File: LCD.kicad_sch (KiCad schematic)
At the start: 13 parts, among them IC3 LED_Driver_TPS61165DBVR, J5 IM2_Jumper, J6 IM1_Jumper, J8 IM0_Jumper

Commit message: Update
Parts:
- C30, C33, C40, C41, C52: footprint Capacitor_SMD:C_0805_2012Metric_Pad1.18x1.45mm_HandSolder -> Capacitor_SMD:C_0805_2012Metric
- R10: footprint Resistor_SMD:R_0805_2012Metric_Pad1.20x1.40mm_HandSolder -> Resistor_SMD:R_0805_2012Metric_1
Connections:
- net +3.3V is gone; now on net 3V3_BK4+: J5.1 (Pin_1), J6.1 (Pin_1), J8.1 (Pin_1)
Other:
- note added: "VCC"
- note added: "VCCIO"

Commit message: Update
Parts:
- removed C30: 1u, Capacitor_SMD:C_0805_2012Metric, symbol Device:C
- removed C33, C52: 4u7, Capacitor_SMD:C_0805_2012Metric, symbol Device:C
- removed C40: 220n, Capacitor_SMD:C_0805_2012Metric, symbol Device:C
- removed C41: 100n, Capacitor_SMD:C_0805_2012Metric, symbol Device:C
- removed D3: MBR0540T1G, Personal_Project:MBR0540T3G_SOD3716X135N, symbol Device:D
- removed FFC1: FFC_ZF5S-40-02-T-WT, Personal_Project:FFC_ZF5S-40-02-T-WT, symbol Personal_Projects:FFC_ZF5S-40-02-T-WT
- removed IC3: LED_Driver_TPS61165DBVR, Personal_Project:LEDDriver_TPS61165DBVR_SOT95P280X145-6N, symbol Personal_Projects:LED_Driver_TPS61165DBVR
- removed J5: IM2_Jumper, Connector_PinHeader_2.54mm:PinHeader_1x03_P2.54mm_Vertical, symbol Connector_Generic:Conn_01x03
- removed J6: IM1_Jumper, Connector_PinHeader_2.54mm:PinHeader_1x03_P2.54mm_Vertical, symbol Connector_Generic:Conn_01x03
- removed J8: IM0_Jumper, Connector_PinHeader_2.54mm:PinHeader_1x03_P2.54mm_Vertical, symbol Connector_Generic:Conn_01x03
- removed L1: Inductor_VLCF5020T-100M1R1-1, Personal_Project:Inductor_VLCF5020, symbol Personal_Projects:Inductor_VLCF5020T-100M1R1-1
- removed R10: 1R8, Resistor_SMD:R_0805_2012Metric_1, symbol Device:R
- added J9: BTB_10132798-062100LF, Personal_Project:BTB_AMPHENOL_10132798-062100LF, symbol Personal_Projects:BTB_10132798-062100LF
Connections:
- net 3V3_BK4+: now also J9.59, J9.60
- net FMC_A0: now also J9.30
- net FMC_D0: now also J9.10
- net FMC_D1: now also J9.11
- net FMC_D10: now also J9.24
- net FMC_D11: now also J9.25
- net FMC_D12: now also J9.1
- net FMC_D13: now also J9.2
- net FMC_D14: now also J9.3
- net FMC_D15: now also J9.5
- net FMC_D2: now also J9.13
- net FMC_D3: now also J9.14
- net FMC_D4: now also J9.16
- net FMC_D5: now also J9.17
- net FMC_D6: now also J9.18
- net FMC_D7: now also J9.20
- net FMC_D8: now also J9.21
- net FMC_D9: now also J9.22
- net FMC_NE1: now also J9.29
- net FMC_NOE: now also J9.6
- net FMC_NWE: now also J9.26
- net GND: now also J9.12, J9.15, J9.19, J9.23, J9.27, J9.31, J9.32, J9.33, J9.34, J9.35, J9.36, J9.37, J9.38, J9.39, J9.4, J9.40, J9.41, J9.42, J9.43, J9.44, J9.45, J9.46, J9.47, J9.48, J9.49, J9.50, J9.51, J9.52, J9.53, J9.54, J9.55, J9.56, J9.57, J9.58, J9.9, J9.SH1, J9.SH2
- net LCD_RESET: now also J9.7
- net LCD_TE: now also J9.28
- net LED_Driver_CTRL: now also J9.8
- no-connect marks 6 -> 0
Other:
- note removed: "CTRL PIN (Dimming mode - digital) The default dimming mode is PWM dimming. To enter 1 wire mode, the following digital pattern on the CTRL pin must be recognized by the device every time the device starts from the shutdown mode. 1. Pull CTRL pin high to enable the TPS61165, and to start the 1wire detection window. 2. After the EasyScale detection delay (tes_delay, 100 μs) expires, drive CTRL low 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"
- note removed: "Chip Selection Pin"
- note removed: "Compared to TN (Twisted Nematic) displays, IPS panels look much better when viewed from the side or at an angle - which is important for user interfaces on handheld or embedded devices. TE Pin When enabled via a command (usually 0x35), the TE pin outputs a pulse or level: Rising edge or level indicates it's safe to update GRAM (internal display RAM). You can wait for TE before sending new pixel d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"
- note removed: "Connect TE to a GPIO or external interrupt pin"
- note removed: "Connector for www.aliexpress.com/item/1005008632320232.html ILI9488 LCD, SSD1963"
- note removed: "Display Data/Command Selection Pin (L:Command, H: Data)"
- note removed: "IM0, IM1, IM2 to set the interface mode 8080 parallel or SPI"
- note removed: "MBR0540T1G"
- note removed: "NC Using capacitive touch"
- note removed: "R_SET = 200 mV / 120 mA = 1.67 Ω (use 1.6 Ω or 1.8 Ω standard)"
- note removed: "Read Enable In MCU Parallel Interface"
- note removed: "SOT-23"
- note removed: "To GPIO"
- note removed: "VCC"
- note removed: "VCCIO"
- note removed: "Was 5V on reference design"
- note removed: "Write Enable In MCU Parallel Interface"

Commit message: Update
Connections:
- net FMC_A0 is gone; now on net FMC_D7: J9.30
- net FMC_NE1 is gone; now on net FMC_D6: J9.29
- net FMC_D1: now also J9.12; no longer J9.11
- net FMC_D10: now also J9.56; no longer J9.24
- net FMC_D11: now also J9.52; no longer J9.25
- net FMC_D2: now also J9.14; no longer J9.13
- net FMC_D3: now also J9.16; no longer J9.14
- net FMC_D4: now also J9.22; no longer J9.16
- net FMC_D5: now also J9.24; no longer J9.17
- net FMC_D6: no longer J9.18
- net FMC_D7: no longer J9.20
- net FMC_D8: now also J9.59; no longer J9.21
- net FMC_D9: now also J9.58; no longer J9.22
- net FMC_NOE: now also J9.35; no longer J9.6
- net FMC_NWE: now also J9.27; no longer J9.26
- net GND: now also J9.11, J9.13, J9.17, J9.21, J9.25, J9.26, J9.28, J9.6; no longer J9.12, J9.19, J9.27, J9.31, J9.33, J9.35, J9.52, J9.56, J9.58
- net LCD_TE: now also J9.33; no longer J9.28
- net LED_Driver_CTRL: now also J9.31; no longer J9.8
- net 3V3_BK4+ renamed FMC_NE3
- net FMC_NE3: no longer J9.59
- new net FMC_A9: J9.8
- new net SMPS_OUT2_3V3+: J9.18, J9.19, J9.20

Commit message: Update
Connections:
- net GND: now also J9.7; no longer J9.46
- net LCD_RESET: now also J9.46; no longer J9.7
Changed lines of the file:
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@@
+	)
+	(junction
+		(at 176.53 113.03)
+		(diameter 0)
+		(color 0 0 0 0)
 	)
 	(junction
@@
 	)
 	(junction
-		(at 259.08 135.89)
-		(diameter 0)
-		(color 0 0 0 0)
-	)
-	(junction
 		(at 259.08 171.45)
 		(diameter 0)
@@
 	(wire
 		(pts
-			(xy 214.63 135.89) (xy 259.08 135.89)
-		)
-		(stroke
-			(width 0)
-			(type default)
-		)
-	)
-	(wire
-		(pts
 			(xy 199.39 179.07) (xy 199.39 181.61)
 		)
@@
 	(wire
 		(pts
-			(xy 259.08 135.89) (xy 259.08 138.43)
+			(xy 259.08 133.35) (xy 259.08 138.43)
 		)
 		(stroke
@@
 	(wire
 		(pts
-			(xy 259.08 133.35) (xy 259.08 135.89)
+			(xy 214.63 135.89) (xy 229.87 135.89)
 		)
 		(stroke
@@
 	(wire
 		(pts
+			(xy 176.53 113.03) (xy 176.53 115.57)
+		)
+		(stroke
+			(width 0)
+			(type default)
+		)
+	)
+	(wire
+		(pts
 			(xy 259.08 181.61) (xy 259.08 182.88)
 		)
@@
 	(wire
 		(pts
-			(xy 189.23 115.57) (xy 172.72 115.57)
+			(xy 189.23 115.57) (xy 176.53 115.57)
 		)
 		(stroke
@@
 	(wire
 		(pts
+			(xy 176.53 113.03) (xy 172.72 113.03)
+		)
+		(stroke
+			(width 0)
+			(type default)
+		)
+	)
+	(wire
+		(pts
 			(xy 259.08 140.97) (xy 259.08 143.51)
 		)
@@
 	(wire
 		(pts
-			(xy 189.23 113.03) (xy 172.72 113.03)
+			(xy 189.23 113.03) (xy 176.53 113.03)
 		)
 		(stroke
@@
 		)
 	)
+	(label "LCD_RESET"
+		(at 229.87 135.89 180)
+		(fields_autoplaced yes)
+		(effects
+			(font
+				(size 1.27 1.27)
+			)
+			(justify right bottom)
+		)
+	)
 	(label "FMC_D7"
 		(at 172.72 173.99 0)
@@
 	(label "FMC_D12"
 		(at 172.72 100.33 0)
-		(fields_autoplaced yes)
-		(effects
-			(font
-				(size 1.27 1.27)
-			)
-			(justify left bottom)
-		)
-	)
-	(label "LCD_RESET"
-		(at 172.72 115.57 0)
 		(fields_autoplaced yes)
 		(effects
@@
 	(hierarchical_label "LCD_RESET"
 		(shape bidirectional)
-		(at 172.72 115.57 180)
-		(fields_autoplaced yes)
-		(effects
-			(font
-				(size 1.27 1.27)
-			)
-			(justify right)
-		)
-	)
+		(at 229.87 135.89 0)
+		(fields_autoplaced yes)
+		(effects
+			(font
+				(size 1.27 1.27)
+			)
+			(justify left)
+		)
+	)

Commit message: Update
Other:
- company: (none) -> Peter Hancak
- title: (none) -> STM32H7S3 Board
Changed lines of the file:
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@@
 	(generator_version "8.0")
 	(paper "A3")
+	(title_block
+		(title "STM32H7S3 Board")
+		(date "2026-03-17")
+		(rev "B")
+		(company "Peter Hancak")
+	)
 	(junction
 		(at 259.08 151.13)

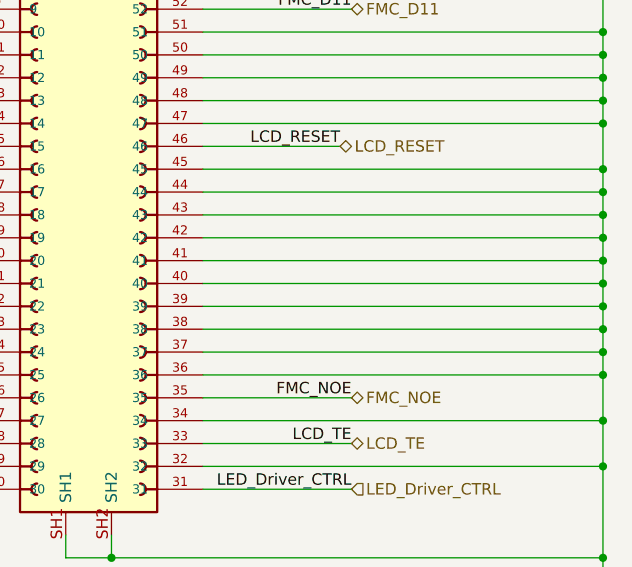
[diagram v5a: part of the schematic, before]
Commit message: Added I2C to the LCD interface
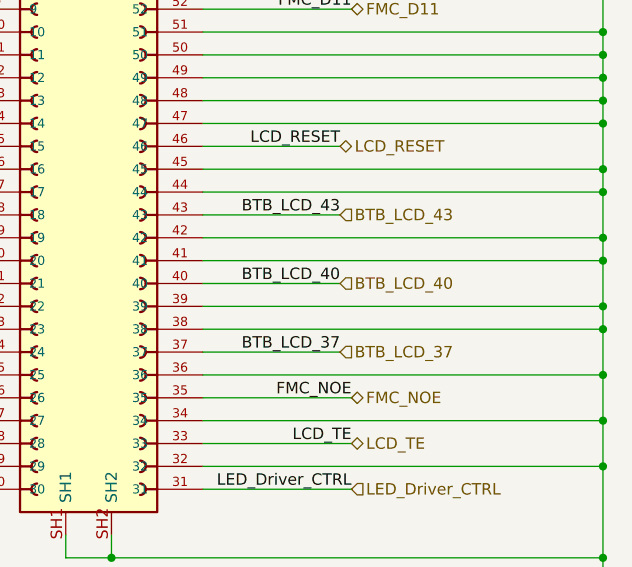
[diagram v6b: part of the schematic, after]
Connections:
- net GND: no longer J9.37, J9.40, J9.43
- new net BTB_LCD_37: J9.37
- new net BTB_LCD_40: J9.40
- new net BTB_LCD_43: J9.43
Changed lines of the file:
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@@
-	)
-	(junction
-		(at 259.08 151.13)
-		(diameter 0)
-		(color 0 0 0 0)
 	)
 	(junction
@@
 	)
 	(junction
-		(at 259.08 143.51)
-		(diameter 0)
-		(color 0 0 0 0)
-	)
-	(junction
 		(at 259.08 118.11)
 		(diameter 0)
@@
 	)
 	(junction
-		(at 259.08 158.75)
-		(diameter 0)
-		(color 0 0 0 0)
-	)
-	(junction
 		(at 259.08 153.67)
 		(diameter 0)
@@
 	(wire
 		(pts
-			(xy 259.08 158.75) (xy 259.08 161.29)
+			(xy 259.08 156.21) (xy 259.08 161.29)
 		)
 		(stroke
@@
 	(wire
 		(pts
+			(xy 214.63 143.51) (xy 229.87 143.51)
+		)
+		(stroke
+			(width 0)
+			(type default)
+		)
+	)
+	(wire
+		(pts
 			(xy 199.39 179.07) (xy 199.39 181.61)
 		)
@@
 	(wire
 		(pts
-			(xy 259.08 143.51) (xy 259.08 146.05)
-		)
-		(stroke
-			(width 0)
-			(type default)
-		)
-	)
-	(wire
-		(pts
 			(xy 189.23 107.95) (xy 172.72 107.95)
 		)
@@
 	(wire
 		(pts
-			(xy 259.08 151.13) (xy 259.08 153.67)
-		)
-		(stroke
-			(width 0)
-			(type default)
-		)
-	)
-	(wire
-		(pts
-			(xy 214.63 151.13) (xy 259.08 151.13)
+			(xy 259.08 148.59) (xy 259.08 153.67)
 		)
 		(stroke
@@
 	(wire
 		(pts
+			(xy 214.63 158.75) (xy 229.87 158.75)
+		)
+		(stroke
+			(width 0)
+			(type default)
+		)
+	)
+	(wire
+		(pts
 			(xy 189.23 110.49) (xy 172.72 110.49)
 		)
@@
 	(wire
 		(pts
+			(xy 214.63 140.97) (xy 259.08 140.97)
+		)
+		(stroke
+			(width 0)
+			(type default)
+		)
+	)
+	(wire
+		(pts
 			(xy 165.1 148.59) (xy 165.1 146.05)
 		)
@@
 	(wire
 		(pts
-			(xy 214.63 158.75) (xy 259.08 158.75)
-		)
-		(stroke
-			(width 0)
-			(type default)
-		)
-	)
-	(wire
-		(pts
 			(xy 214.63 115.57) (xy 259.08 115.57)
 		)
@@
 	(wire
 		(pts
+			(xy 259.08 140.97) (xy 259.08 146.05)
+		)
+		(stroke
+			(width 0)
+			(type default)
+		)
+	)
+	(wire
+		(pts
 			(xy 189.23 133.35) (xy 172.72 133.35)
 		)
@@
 	(wire
 		(pts
-			(xy 214.63 140.97) (xy 259.08 140.97)
-		)
-		(stroke
-			(width 0)
-			(type default)
-		)
-	)
-	(wire
-		(pts
 			(xy 214.63 168.91) (xy 231.14 168.91)
 		)
@@
 	(wire
 		(pts
-			(xy 214.63 143.51) (xy 259.08 143.51)
-		)
-		(stroke
-			(width 0)
-			(type default)
-		)
-	)
-	(wire
-		(pts
 			(xy 204.47 179.07) (xy 204.47 181.61)
 		)
@@
 	(wire
 		(pts
+			(xy 176.53 113.03) (xy 172.72 113.03)
+		)
+		(stroke
+			(width 0)
+			(type default)
+		)
+	)
+	(wire
+		(pts
 			(xy 259.08 138.43) (xy 259.08 140.97)
 		)
@@
 	(wire
 		(pts
-			(xy 259.08 148.59) (xy 259.08 151.13)
-		)
-		(stroke
-			(width 0)
-			(type default)
-		)
-	)
-	(wire
-		(pts
-			(xy 259.08 156.21) (xy 259.08 158.75)
-		)
-		(stroke
-			(width 0)
-			(type default)
-		)
-	)
-	(wire
-		(pts
-			(xy 176.53 113.03) (xy 172.72 113.03)
-		)
-		(stroke
-			(width 0)
-			(type default)
-		)
-	)
-	(wire
-		(pts
-			(xy 259.08 140.97) (xy 259.08 143.51)
-		)
-		(stroke
-			(width 0)
-			(type default)
-		)
-	)
-	(wire
-		(pts
 			(xy 189.23 173.99) (xy 172.72 173.99)
 		)
@@
 		(pts
 			(xy 189.23 113.03) (xy 176.53 113.03)
+		)
+		(stroke
+			(width 0)
+			(type default)
+		)
+	)
+	(wire
+		(pts
+			(xy 214.63 151.13) (xy 229.87 151.13)
 		)
 		(stroke
@@
 		)
 	)
+	(label "BTB_LCD_43"
+		(at 229.87 143.51 180)
+		(fields_autoplaced yes)
+		(effects
+			(font
+				(size 1.27 1.27)
+			)
+			(justify right bottom)
+		)
+	)
 	(label "FMC_D3"
 		(at 172.72 138.43 0)
@@
 		)
 	)
+	(label "BTB_LCD_40"
+		(at 229.87 151.13 180)
+		(fields_autoplaced yes)
+		(effects
+			(font
+				(size 1.27 1.27)
+			)
+			(justify right bottom)
+		)
+	)
 	(label "FMC_D4"
 		(at 172.72 153.67 0)
@@
 			)
 			(justify left bottom)
+		)
+	)
+	(label "BTB_LCD_37"
+		(at 229.87 158.75 180)
+		(fields_autoplaced yes)
+		(effects
+			(font
+				(size 1.27 1.27)
+			)
+			(justify right bottom)
 		)
 	)
@@
 		)
 	)
+	(hierarchical_label "BTB_LCD_43"
+		(shape input)
+		(at 229.87 143.51 0)
+		(fields_autoplaced yes)
+		(effects
+			(font
+				(size 1.27 1.27)
+			)
+			(justify left)
+		)
+	)
+	(hierarchical_label "BTB_LCD_40"
+		(shape input)
+		(at 229.87 151.13 0)
+		(fields_autoplaced yes)
+		(effects
+			(font
+				(size 1.27 1.27)
+			)
+			(justify left)
+		)
+	)
 	(hierarchical_label "FMC_D8"
 		(shape bidirectional)
@@
 		)
 	)
+	(hierarchical_label "BTB_LCD_37"
+		(shape input)
+		(at 229.87 158.75 0)
+		(fields_autoplaced yes)
+		(effects
+			(font
+				(size 1.27 1.27)
+			)
+			(justify left)
+		)
+	)
